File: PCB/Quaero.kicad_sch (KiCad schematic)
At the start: 69 parts, among them J1 USB_C_Receptacle_USB2.0_16P, J2 OLED_128x32, U1 RP2040_Zero

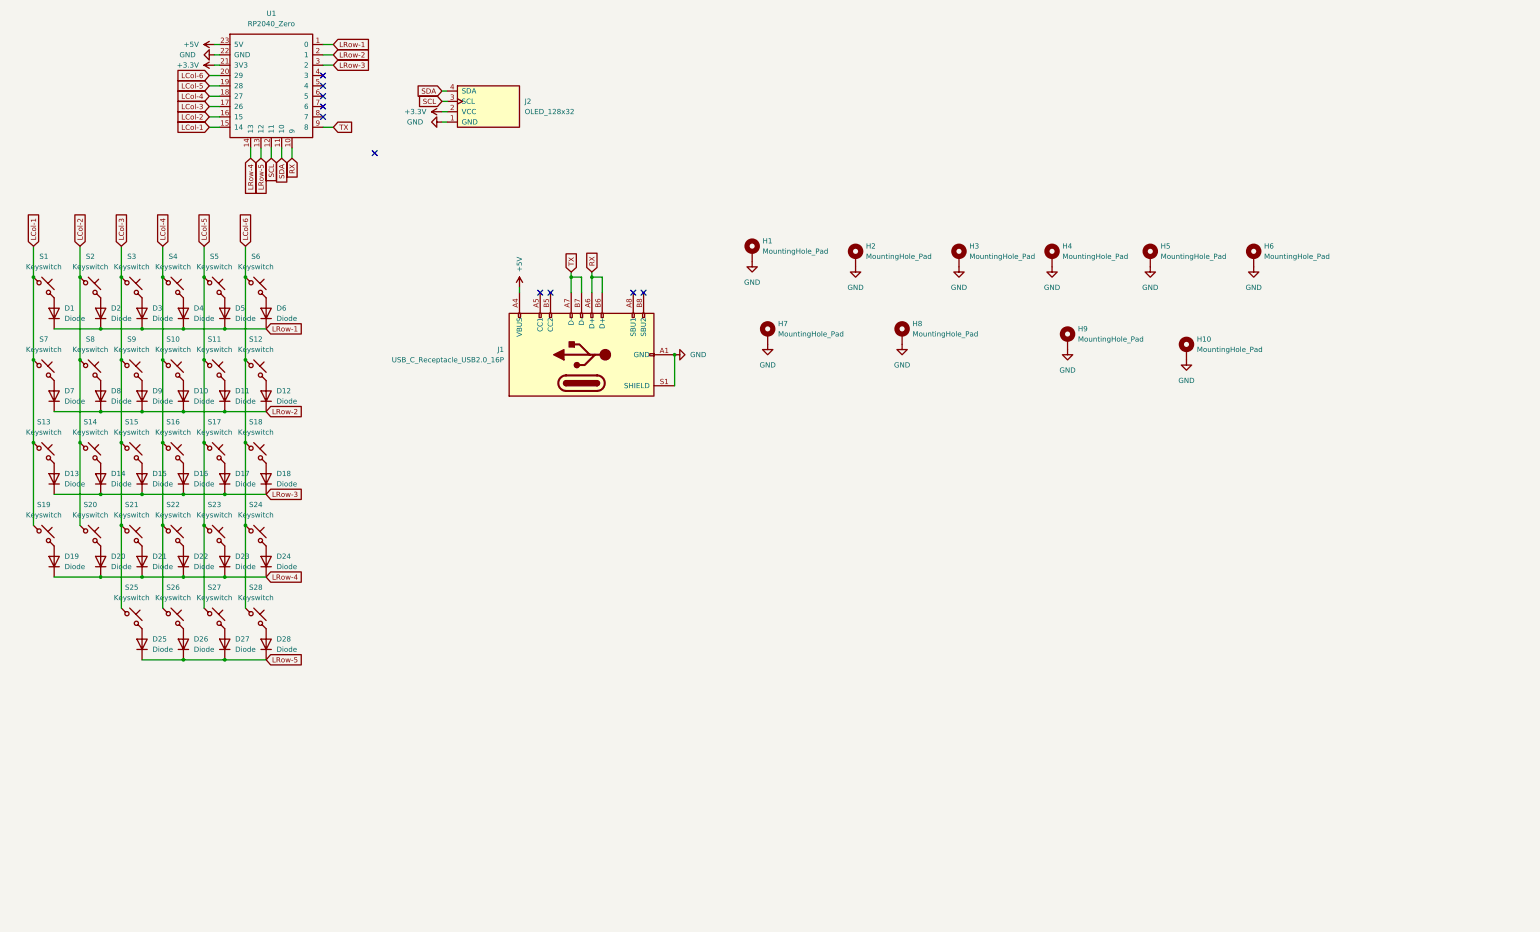
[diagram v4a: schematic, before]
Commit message: Finished right side
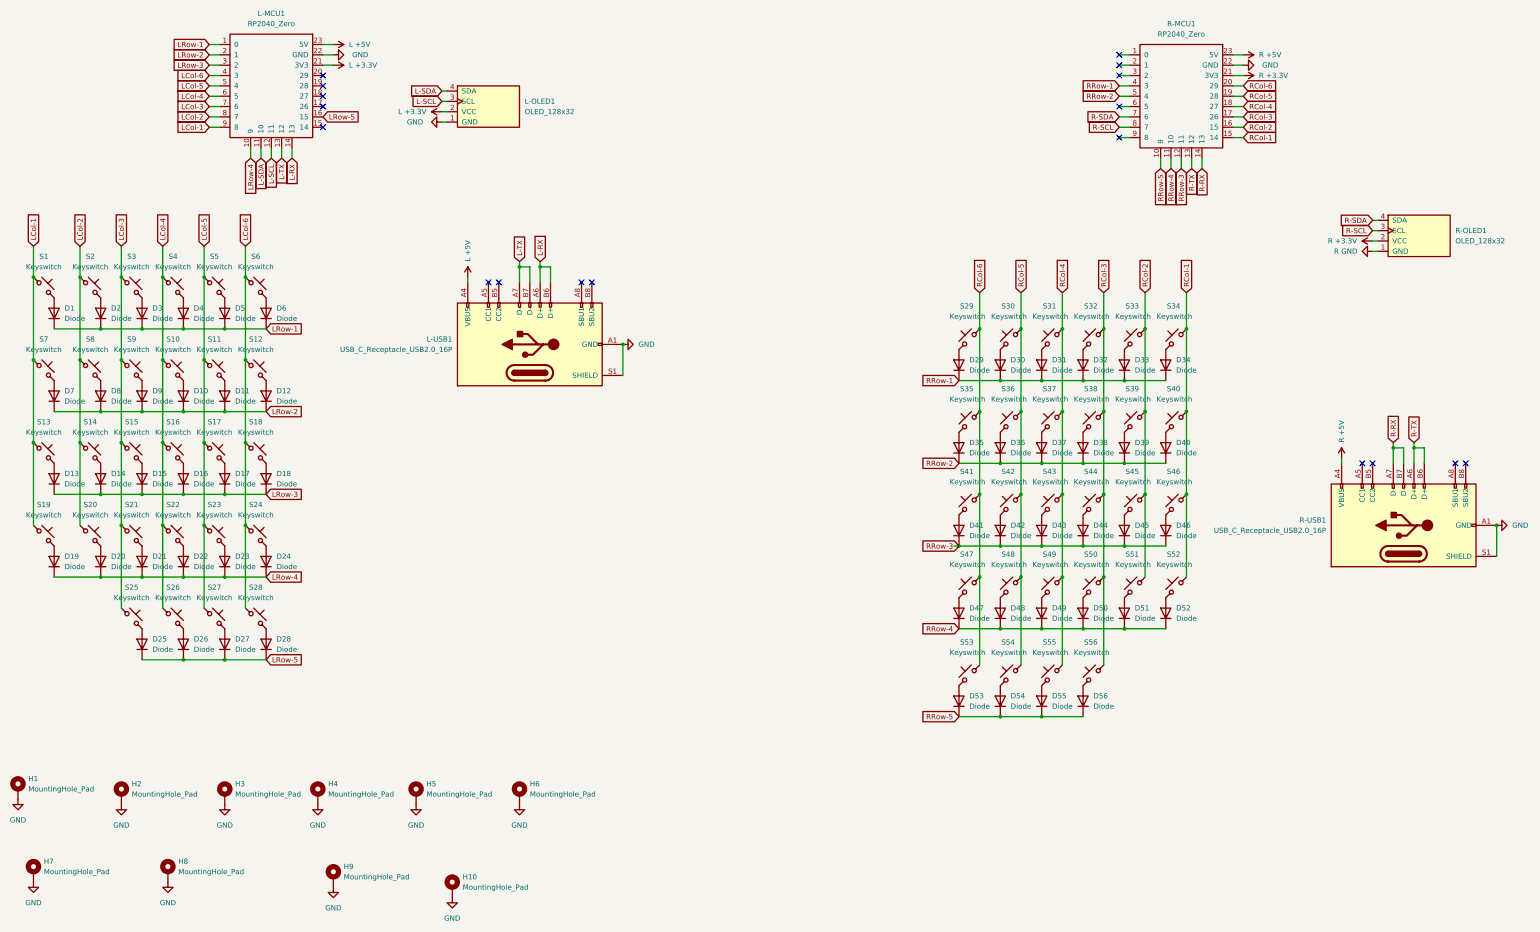
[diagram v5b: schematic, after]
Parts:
- added D29, D30, D31, D32, D33, D34, D35, D36, D37, D38, D39, D40, D41, D42, D43, D44, D45, D46, D47, D48, D49, D50, D51, D52, D53, D54, D55, D56: Diode, symbol ScottoKeebs:Placeholder_Diode
- added R-MCU1: RP2040_Zero, ScottoKeebs_MCU:RP2040_Zero_Flipped, symbol ScottoKeebs:MCU_RP2040_Zero
- added R-OLED1: OLED_128x32, ScottoKeebs_Components:OLED_128x32, symbol ScottoKeebs:OLED_128x32
- added R-USB1: USB_C_Receptacle_USB2.0_16P, Connector_USB:USB_C_Receptacle_GCT_USB4085, symbol Connector:USB_C_Receptacle_USB2.0_16P
- added S29, S30, S31, S32, S33, S34, S35, S36, S37, S38, S39, S40, S41, S42, S43, S44, S45, S46, S47, S48, S49, S50, S51, S52, S53, S54, S55, S56: Keyswitch, symbol ScottoKeebs:Placeholder_Keyswitch
- L-MCU1: renamed from U1; footprint ScottoKeebs_MCU:RP2040_Zero -> ScottoKeebs_MCU:RP2040_Zero_Flipped
- renumbered J2 to L-OLED1, J1 to L-USB1
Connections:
- net GND: now also R-MCU1.22 (GND), R-USB1.A1 (GND), R-USB1.A12 (GND), R-USB1.B1 (GND), R-USB1.B12 (GND), R-USB1.S1 (SHIELD)
- net LCol-1: now also L-MCU1.9 (8); no longer L-MCU1.15 (14)
- net LCol-2: now also L-MCU1.8 (7); no longer L-MCU1.16 (15)
- net LCol-3: now also L-MCU1.7 (6); no longer L-MCU1.17 (26)
- net LCol-4: now also L-MCU1.6 (5); no longer L-MCU1.18 (27)
- net LCol-5: now also L-MCU1.5 (4); no longer L-MCU1.19 (28)
- net LCol-6: now also L-MCU1.4 (3); no longer L-MCU1.20 (29)
- net LRow-4: now also L-MCU1.10 (9); no longer L-MCU1.14 (13)
- net LRow-5: now also L-MCU1.16 (15); no longer L-MCU1.13 (12)
- net +3.3V renamed L +3.3V
- net +5V renamed L +5V
- net RX renamed L-RX
- net L-RX: now also L-MCU1.14 (13); no longer L-MCU1.10 (9)
- net SCL renamed L-SCL
- net SDA renamed L-SDA
- net TX renamed L-TX
- net L-TX: now also L-MCU1.13 (12); no longer L-MCU1.9 (8)
- new net: D39.2 (A), S39.1
- new net: D48.2 (A), S48.1
- new net: D41.2 (A), S41.1
- new net: D53.2 (A), S53.1
- new net: D35.2 (A), S35.1
- new net: D47.2 (A), S47.1
- new net: D51.2 (A), S51.1
- new net: D37.2 (A), S37.1
- new net: D38.2 (A), S38.1
- new net: D29.2 (A), S29.1
- new net: D34.2 (A), S34.1
- new net: D45.2 (A), S45.1
- new net: D44.2 (A), S44.1
- new net: D40.2 (A), S40.1
- new net: D52.2 (A), S52.1
- new net: D56.2 (A), S56.1
- new net: D54.2 (A), S54.1
- new net: D49.2 (A), S49.1
- new net: D30.2 (A), S30.1
- new net: D50.2 (A), S50.1
- new net: D46.2 (A), S46.1
- new net: D31.2 (A), S31.1
- new net: D32.2 (A), S32.1
- new net: D55.2 (A), S55.1
- new net: D43.2 (A), S43.1
- new net: D42.2 (A), S42.1
- new net: D33.2 (A), S33.1
- new net: D36.2 (A), S36.1
- new net R +3.3V: R-MCU1.21 (3V3), R-OLED1.2 (VCC)
- new net R +5V: R-MCU1.23 (5V), R-USB1.A4 (VBUS), R-USB1.A9 (VBUS), R-USB1.B4 (VBUS), R-USB1.B9 (VBUS)
- new net R GND: R-OLED1.1 (GND)
- new net R-RX: R-MCU1.14 (13), R-USB1.A7 (D-), R-USB1.B7 (D-)
- new net R-SCL: R-MCU1.8 (7), R-OLED1.3 (SCL)
- new net R-SDA: R-MCU1.7 (6), R-OLED1.4 (SDA)
- new net R-TX: R-MCU1.13 (12), R-USB1.A6 (D+), R-USB1.B6 (D+)
- new net RCol-1: R-MCU1.15 (14), S34.2, S40.2, S46.2, S52.2
- new net RCol-2: R-MCU1.16 (15), S33.2, S39.2, S45.2, S51.2
- new net RCol-3: R-MCU1.17 (26), S32.2, S38.2, S44.2, S50.2, S56.2
- new net RCol-4: R-MCU1.18 (27), S31.2, S37.2, S43.2, S49.2, S55.2
- new net RCol-5: R-MCU1.19 (28), S30.2, S36.2, S42.2, S48.2, S54.2
- new net RCol-6: R-MCU1.20 (29), S29.2, S35.2, S41.2, S47.2, S53.2
- new net RRow-1: D29.1 (K), D30.1 (K), D31.1 (K), D32.1 (K), D33.1 (K), D34.1 (K), R-MCU1.4 (3)
- new net RRow-2: D35.1 (K), D36.1 (K), D37.1 (K), D38.1 (K), D39.1 (K), D40.1 (K), R-MCU1.5 (4)
- new net RRow-3: D41.1 (K), D42.1 (K), D43.1 (K), D44.1 (K), D45.1 (K), D46.1 (K), R-MCU1.12 (11)
- new net RRow-4: D47.1 (K), D48.1 (K), D49.1 (K), D50.1 (K), D51.1 (K), D52.1 (K), R-MCU1.11 (10)
- new net RRow-5: D53.1 (K), D54.1 (K), D55.1 (K), D56.1 (K), R-MCU1.10 (9)
- no-connect marks 10 -> 18
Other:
- moved on the sheet: H1, H10, H2, H3, H4, H5, H6, H7, H8, H9, L-USB1

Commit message: added files + readme improvements
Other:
- moved on the sheet: D1, D10, D11, D12, D13, D14, D15, D16, D17, D18, D19, D2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
